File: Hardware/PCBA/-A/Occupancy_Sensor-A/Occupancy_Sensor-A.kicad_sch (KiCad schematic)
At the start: 66 parts, among them J1 USB_C_Receptacle, J2 Conn_02x05_Odd_Even, Q1 2N7002, Q2 2N7002, Q3 2N7002, Q4 2N7002, Q5 2N7002, SW1 SW_SPDT, SW2 SW_Push, U1 TPS7A0333PDBVR, U2 VL53L8CX, U3 ECMF02-2AMX6, U4 TPS7A03185PDQNR, U5 TCS3430, U6 STM32WB55CGUx, Y1 Crystal_GND24_Small, Y2 Crystal_GND24_Small

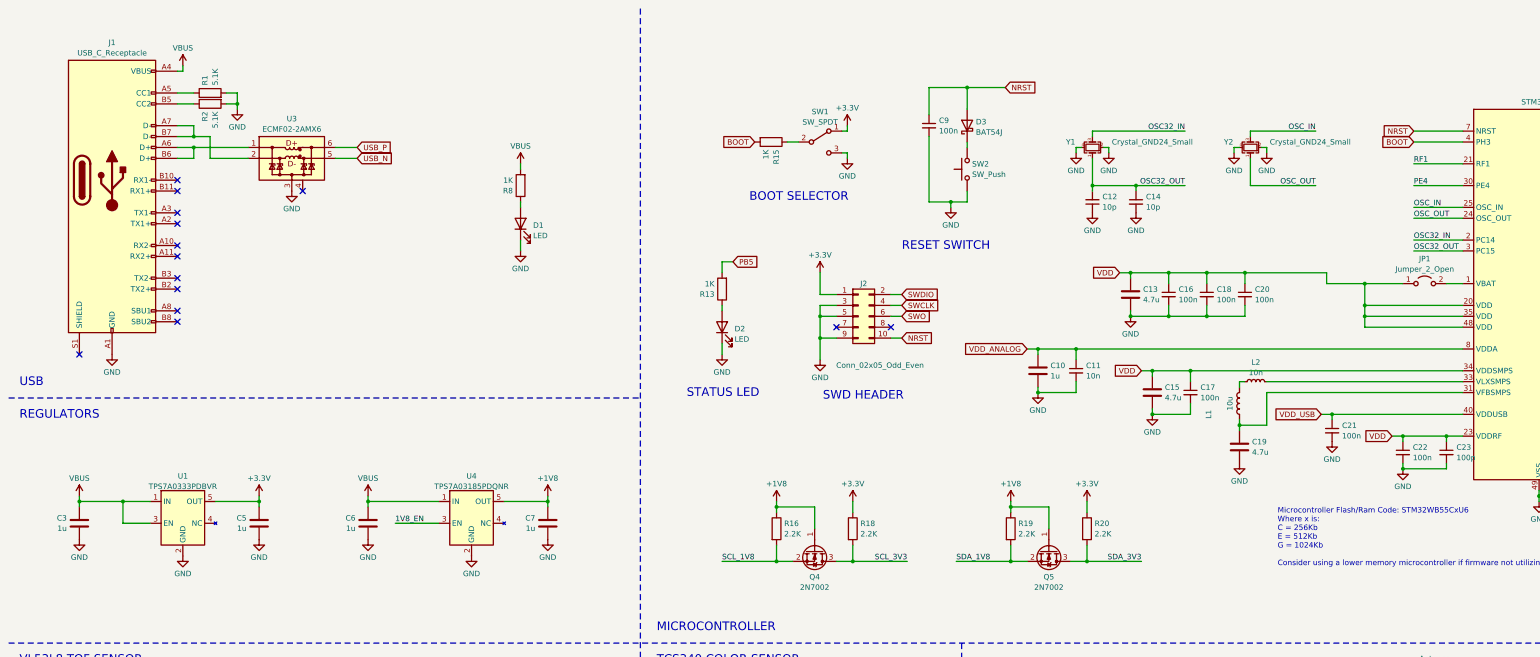
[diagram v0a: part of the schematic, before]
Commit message: General layout, footprint fixes
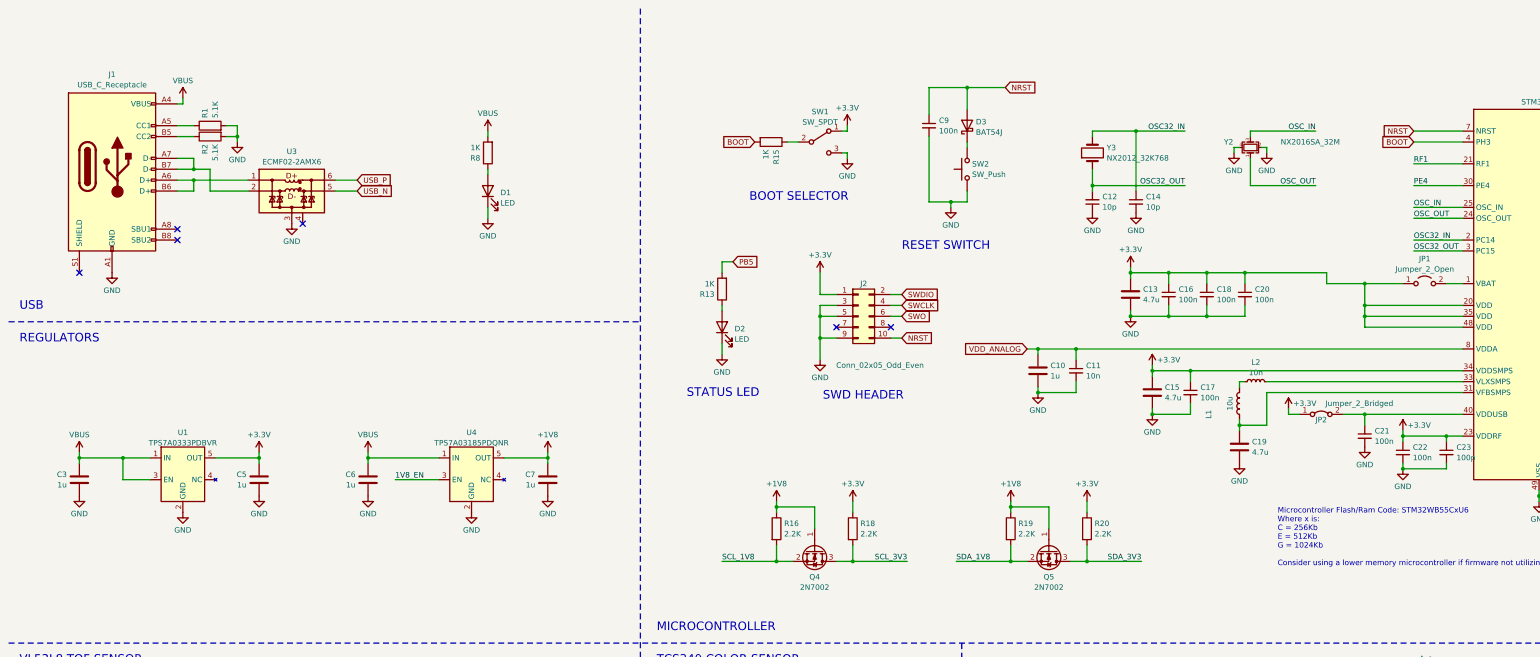
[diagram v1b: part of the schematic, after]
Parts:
- removed Y1: Crystal_GND24_Small, Crystal:Crystal_SMD_SeikoEpson_FA128-4Pin_2.0x1.6mm, symbol Device:Crystal_GND24_Small
- added JP2: Jumper_2_Bridged, Jumper:SolderJumper-2_P1.3mm_Bridged_RoundedPad1.0x1.5mm, symbol Jumper:Jumper_2_Bridged
- added Y3: NX2012_32K768, Occupancy_Sensor_Custom_Footprints:NX2012_32K768, symbol Device:Crystal
- J1: footprint Connector_USB:USB_C_Receptacle_Molex_105450-0101 -> Occupancy_Sensor_Custom_Footprints:TYPEC-304S-ACP16
- JP1: footprint Jumper:SolderJumper-2_P1.3mm_Open_TrianglePad1.0x1.5mm -> Jumper:SolderJumper-2_P1.3mm_Open_RoundedPad1.0x1.5mm
- Y2: value Crystal_GND24_Small -> NX2016SA_32M; footprint Crystal:Crystal_SMD_SeikoEpson_FA128-4Pin_2.0x1.6mm -> Occupancy_Sensor_Custom_Footprints:NX2016SA_32M
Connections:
- net VDD is gone; now on net +3.3V: C13.1, C15.1, C16.1, C17.1, C18.1, C20.1, C22.1, C23.1, JP1.1 (A), U6.20 (VDD), U6.23 (VDDRF), U6.34 (VDDSMPS), U6.35 (VDD), U6.48 (VDD)
- net +3.3V: now also JP2.1 (A)
- net OSC32_IN: now also C14.1, Y3.2
- net OSC32_OUT: now also Y3.1; no longer C14.1
- net VDD_USB: no longer names the net of C21.1, U6.40 (VDDUSB)
- net VDD_USB: now also JP2.2 (B)
- no-connect marks 15 -> 7
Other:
- moved on the sheet: C21, C3, C5, C6, C7, D1, R1, R2, R8, U1, U3, U4

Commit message: Layout, power planes, prelim antenna placement
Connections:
- net PA6 is gone; now on net INT_TOF_3V3: U6.15 (PA6)
- net PA7 is gone; now on net SYNC_3V3: U6.16 (PA7)
- net PA8 is gone; now on net I2C_RST: U6.17 (PA8)
- net PB6 is gone; now on net SCL_3V3: U6.46 (PB6)
- net PB7 is gone; now on net SDA_3V3: U6.47 (PB7)
- net VDD_ANALOG: no longer U6.8 (VDDA)
- net INT_TOF renamed INT_TOF_3V3
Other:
- moved on the sheet: C10, C11, C12, C13, C14, C15, C16, C17, C18, C19, C20, C21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

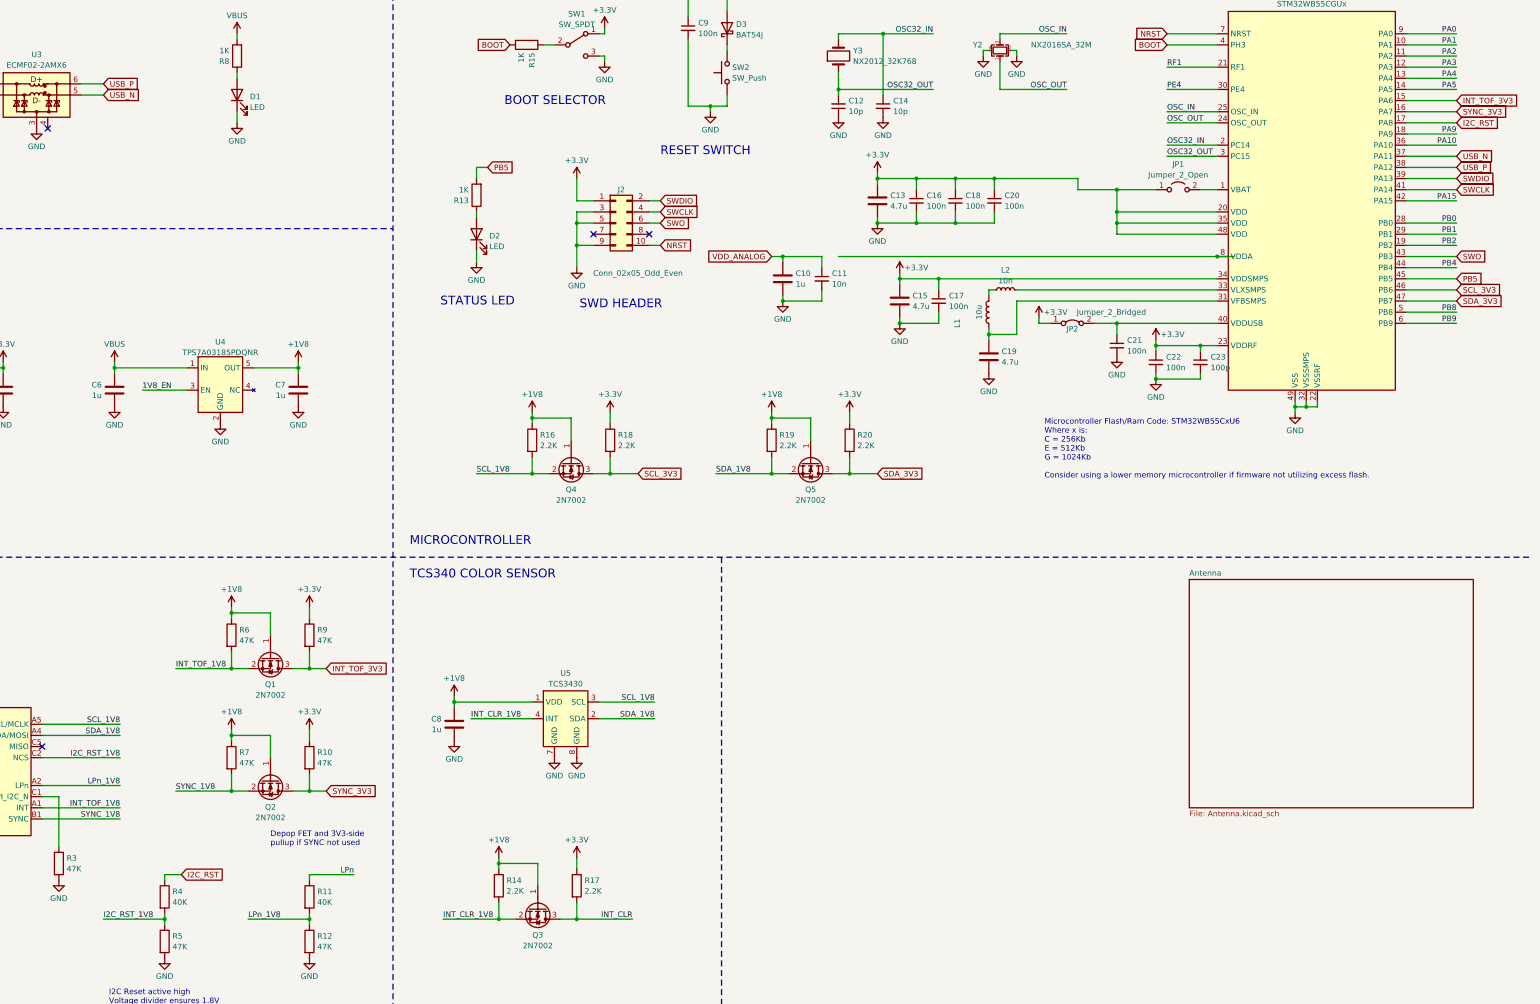
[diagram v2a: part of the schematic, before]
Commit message: Finalize IO pinout, layout
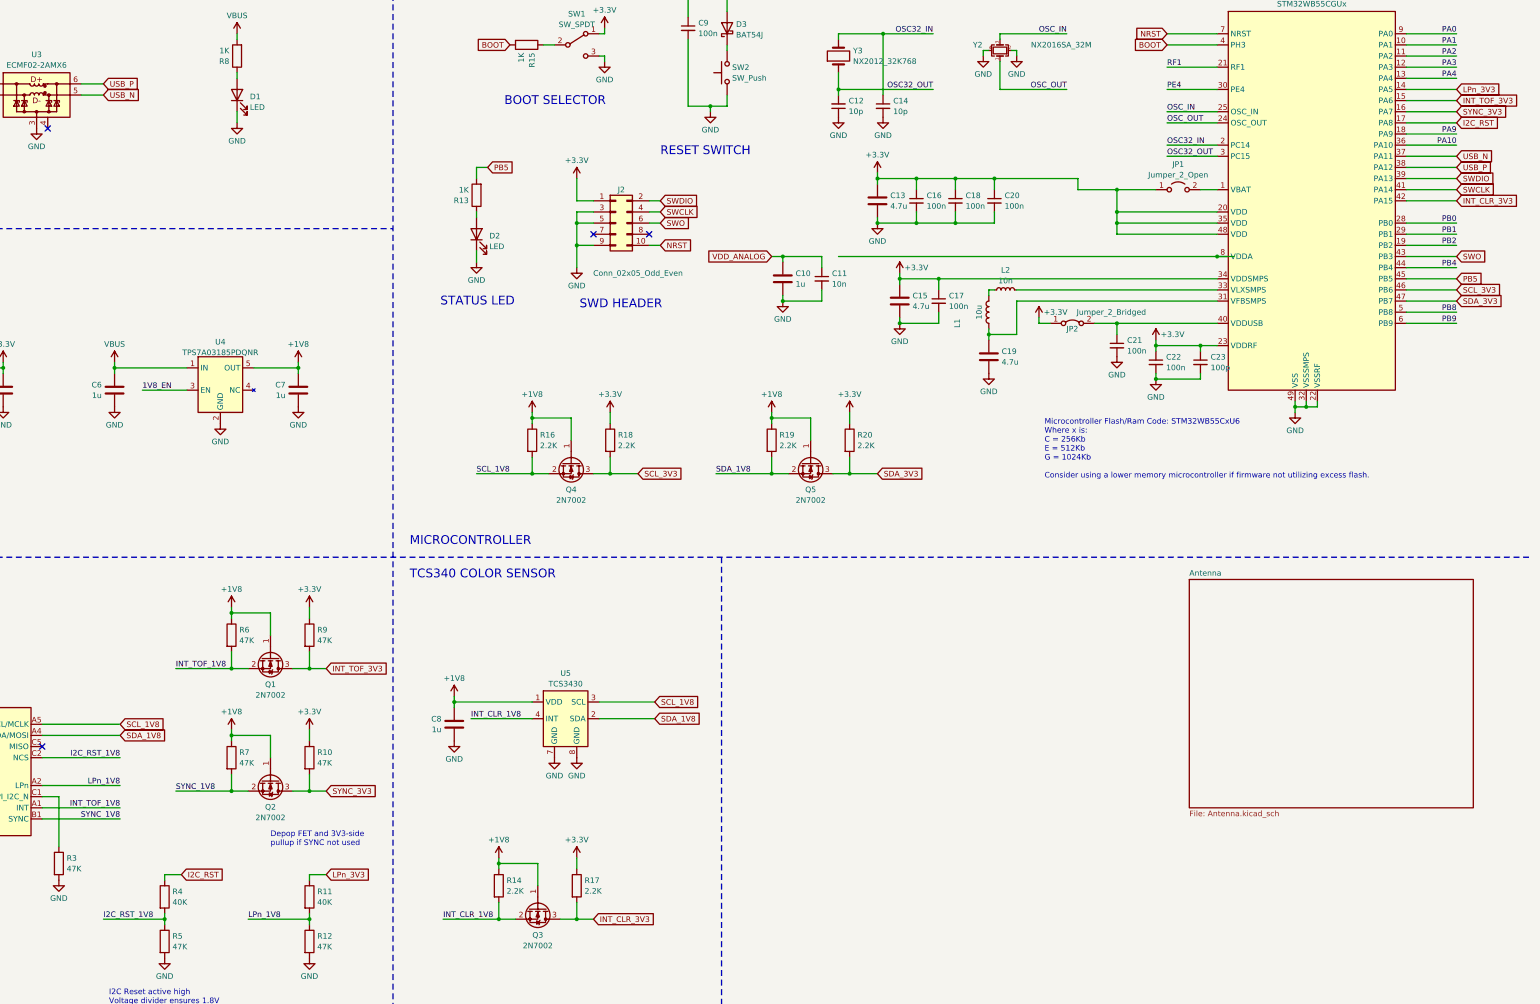
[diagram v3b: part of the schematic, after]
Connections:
- net PA15 is gone; now on net INT_CLR_3V3: U6.42 (PA15)
- net PA5 is gone; now on net LPn_3V3: U6.14 (PA5)
- net INT_CLR renamed INT_CLR_3V3
- net LPn renamed LPn_3V3
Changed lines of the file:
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@@
   (junction (at 138.43 116.84) (diameter 0) (color 0 0 0 0)
   )
+  (junction (at 201.93 242.57) (diameter 0) (color 0 0 0 0)
+  )
   (junction (at 60.96 227.33) (diameter 0) (color 0 0 0 0)
   )
@@
   )
   (junction (at 261.62 53.34) (diameter 0) (color 0 0 0 0)
-  )
-  (junction (at 201.93 242.57) (diameter 0) (color 0 0 0 0)
   )
   (junction (at 248.92 101.6) (diameter 0) (color 0 0 0 0)
@@
     (stroke (width 0) (type default))
   )
-  (wire (pts (xy 201.93 242.57) (xy 214.63 242.57))
-    (stroke (width 0) (type default))
-  )
-  (wire (pts (xy 140.97 232.41) (xy 151.13 232.41))
-    (stroke (width 0) (type default))
-  )
   (wire (pts (xy 39.37 200.66) (xy 39.37 203.2))
     (stroke (width 0) (type default))
@@
     (stroke (width 0) (type default))
   )
+  (wire (pts (xy 140.97 232.41) (xy 144.78 232.41))
+    (stroke (width 0) (type default))
+  )
   (wire (pts (xy 391.16 66.04) (xy 402.59 66.04))
     (stroke (width 0) (type default))
@@
     (stroke (width 0) (type default))
   )
+  (wire (pts (xy 201.93 242.57) (xy 205.74 242.57))
+    (stroke (width 0) (type default))
+  )
   (wire (pts (xy 297.18 99.06) (xy 295.91 99.06))
     (stroke (width 0) (type default))
@@
     (effects (font (size 1.27 1.27)) (justify left bottom))
   )
-  (label "INT_CLR" (at 214.63 242.57 180) (fields_autoplaced)
-    (effects (font (size 1.27 1.27)) (justify right bottom))
-  )
   (label "PB4" (at 402.59 93.98 180) (fields_autoplaced)
     (effects (font (size 1.27 1.27)) (justify right bottom))
@@
     (effects (font (size 1.27 1.27)) (justify left bottom))
   )
-  (label "LPn" (at 151.13 232.41 180) (fields_autoplaced)
-    (effects (font (size 1.27 1.27)) (justify right bottom))
-  )
   (label "RF1" (at 336.55 48.26 0) (fields_autoplaced)
     (effects (font (size 1.27 1.27)) (justify left bottom))
@@
     (effects (font (size 1.27 1.27)) (justify left bottom))
   )
-  (label "SDA_1V8" (at 97.79 200.66 180) (fields_autoplaced)
-    (effects (font (size 1.27 1.27)) (justify right bottom))
-  )
-  (label "SCL_1V8" (at 219.71 193.04 180) (fields_autoplaced)
-    (effects (font (size 1.27 1.27)) (justify right bottom))
-  )
   (label "LPn_1V8" (at 97.79 212.09 180) (fields_autoplaced)
     (effects (font (size 1.27 1.27)) (justify right bottom))
@@
     (effects (font (size 1.27 1.27)) (justify left bottom))
   )
-  (label "SDA_1V8" (at 219.71 196.85 180) (fields_autoplaced)
-    (effects (font (size 1.27 1.27)) (justify right bottom))
-  )
   (label "OSC_OUT" (at 313.69 53.34 180) (fields_autoplaced)
     (effects (font (size 1.27 1.27)) (justify right bottom))
@@
     (effects (font (size 1.27 1.27)) (justify right bottom))
   )
-  (label "PA15" (at 402.59 78.74 180) (fields_autoplaced)
-    (effects (font (size 1.27 1.27)) (justify right bottom))
-  )
-  (label "SCL_1V8" (at 97.79 198.12 180) (fields_autoplaced)
-    (effects (font (size 1.27 1.27)) (justify right bottom))
-  )
   (label "OSC32_OUT" (at 283.21 53.34 180) (fields_autoplaced)
     (effects (font (size 1.27 1.27)) (justify right bottom))
@@
   )
   (label "PB1" (at 402.59 86.36 180) (fields_autoplaced)
-    (effects (font (size 1.27 1.27)) (justify right bottom))
-  )
-  (label "PA5" (at 402.59 53.34 180) (fields_autoplaced)
     (effects (font (size 1.27 1.27)) (justify right bottom))
   )
@@
     )
   )
+  (global_label "SCL_1V8" (shape input) (at 219.71 193.04 0) (fields_autoplaced)
+    (effects (font (size 1.27 1.27)) (justify left))
+    (property "Intersheetrefs" "${INTERSHEET_REFS}" (at 230.678 193.04 0)
+      (effects (font (size 1.27 1.27)) (justify left) hide)
+    )
+  )
   (global_label "USB_N" (shape input) (at 93.98 54.61 0) (fields_autoplaced)
     (effects (font (size 1.27 1.27)) (justify left))
@@
     )
   )
+  (global_label "SDA_1V8" (shape input) (at 219.71 196.85 0) (fields_autoplaced)
+    (effects (font (size 1.27 1.27)) (justify left))
+    (property "Intersheetrefs" "${INTERSHEET_REFS}" (at 230.7385 196.85 0)
+      (effects (font (size 1.27 1.27)) (justify left) hide)
+    )
+  )
   (global_label "SWDIO" (shape input) (at 220.98 78.74 0) (fields_autoplaced)
     (effects (font (size 1.27 1.27)) (justify left))
@@
     )
   )
+  (global_label "SDA_1V8" (shape input) (at 97.79 200.66 0) (fields_autoplaced)
+    (effects (font (size 1.27 1.27)) (justify left))
+    (property "Intersheetrefs" "${INTERSHEET_REFS}" (at 108.8185 200.66 0)
+      (effects (font (size 1.27 1.27)) (justify left) hide)
+    )
+  )
+  (global_label "SCL_1V8" (shape input) (at 97.79 198.12 0) (fields_autoplaced)
+    (effects (font (size 1.27 1.27)) (justify left))
+    (property "Intersheetrefs" "${INTERSHEET_REFS}" (at 108.758 198.12 0)
+      (effects (font (size 1.27 1.27)) (justify left) hide)
+    )
+  )
   (global_label "SCL_3V3" (shape input) (at 402.59 99.06 0) (fields_autoplaced)
     (effects (font (size 1.27 1.27)) (justify left))
@@
     )
   )
+  (global_label "INT_CLR_3V3" (shape input) (at 205.74 242.57 0) (fields_autoplaced)
+    (effects (font (size 1.27 1.27)) (justify left))
+    (property "Intersheetrefs" "${INTERSHEET_REFS}" (at 220.639 242.57 0)
+      (effects (font (size 1.27 1.27)) (justify left) hide)
+    )
+  )
   (global_label "INT_TOF_3V3" (shape input) (at 144.78 185.42 0) (fields_autoplaced)
     (effects (font (size 1.27 1.27)) (justify left))
     (property "Intersheetrefs" "${INTERSHEET_REFS}" (at 159.4976 185.42 0)
+      (effects (font (size 1.27 1.27)) (justify left) hide)
+    )
+  )
+  (global_label "LPn_3V3" (shape input) (at 402.59 53.34 0) (fields_autoplaced)
+    (effects (font (size 1.27 1.27)) (justify left))
+    (property "Intersheetrefs" "${INTERSHEET_REFS}" (at 413.4975 53.34 0)
       (effects (font (size 1.27 1.27)) (justify left) hide)
     )
@@
     )
   )
+  (global_label "LPn_3V3" (shape input) (at 144.78 232.41 0) (fields_autoplaced)
+    (effects (font (size 1.27 1.27)) (justify left))
+    (property "Intersheetrefs" "${INTERSHEET_REFS}" (at 155.6875 232.41 0)
+      (effects (font (size 1.27 1.27)) (justify left) hide)
+    )
+  )
   (global_label "PB5" (shape input) (at 402.59 96.52 0) (fields_autoplaced)
     (effects (font (size 1.27 1.27)) (justify left))
@@
       (effects (font (size 1.27 1.27)) (justify left) hide)
     )
+  )
+  (global_label "INT_CLR_3V3" (shape input) (at 402.59 78.74 0) (fields_autoplaced)
+    (effects (font (size 1.27 1.27)) (justify left))
+    (property "Intersheetrefs" "${INTERSHEET_REFS}" (at 417.489 78.74 0)
+      (effects (font (size 1.27 1.27)) (justify left) hide)
+    )
